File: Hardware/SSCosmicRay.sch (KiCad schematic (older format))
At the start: 0 parts

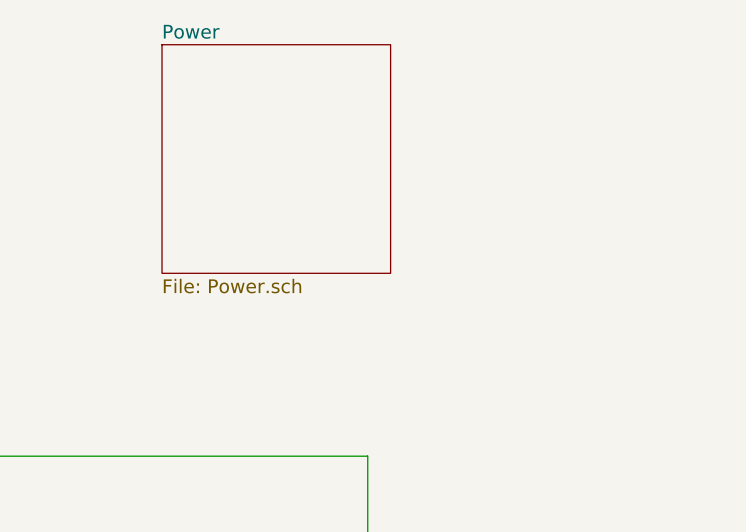
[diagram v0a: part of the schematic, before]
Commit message: Add power section. Switch to smaller pot
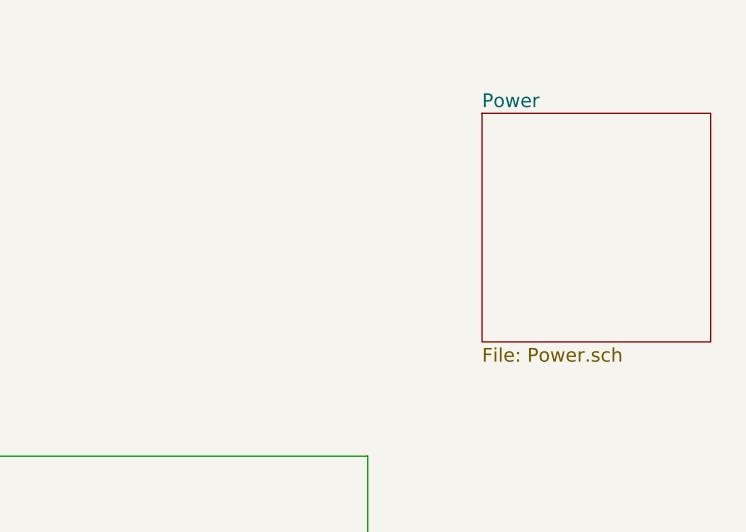
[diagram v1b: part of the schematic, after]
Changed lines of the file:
@@
 $Descr A4 11693 8268
 encoding utf-8
-Sheet 1 7
+Sheet 1 8
 Title "Solid State Cosmic Ray Detector"
 Date "24 sep 2013"
@@
 Connection ~ 5900 4900
 $Sheet
-S 7000 1100 1000 1000
+S 8400 1400 1000 1000
 U 5241F320
 F0 "Power" 60

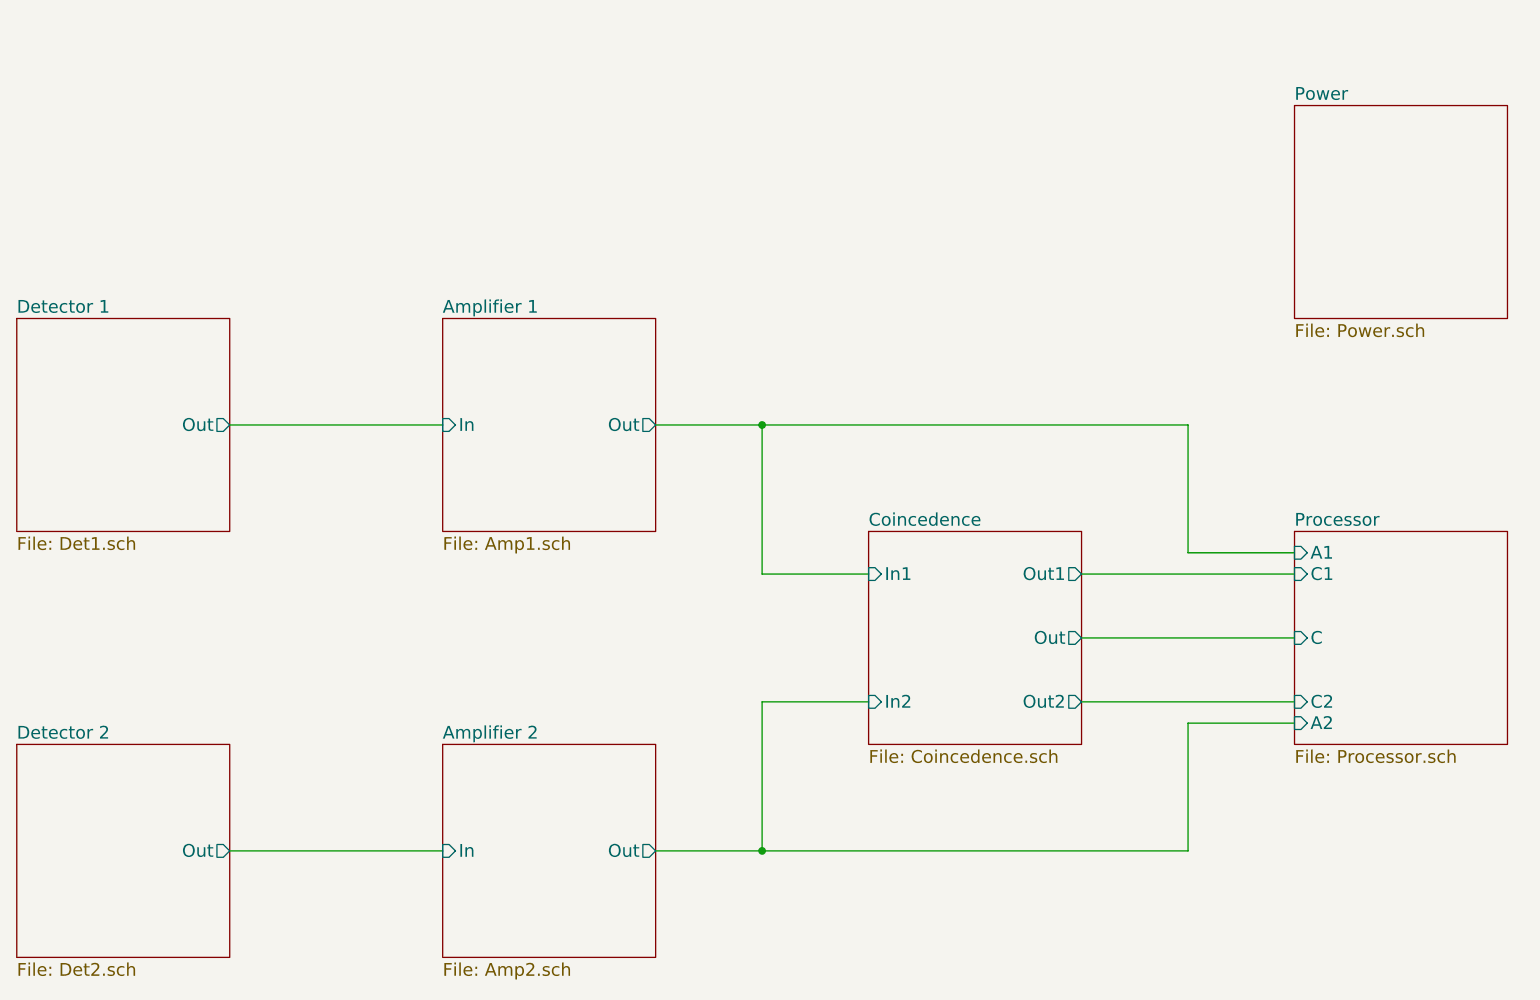
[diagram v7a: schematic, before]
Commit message: Remove coincidence circuitry
PIC32 internal comparator has sufficient performance
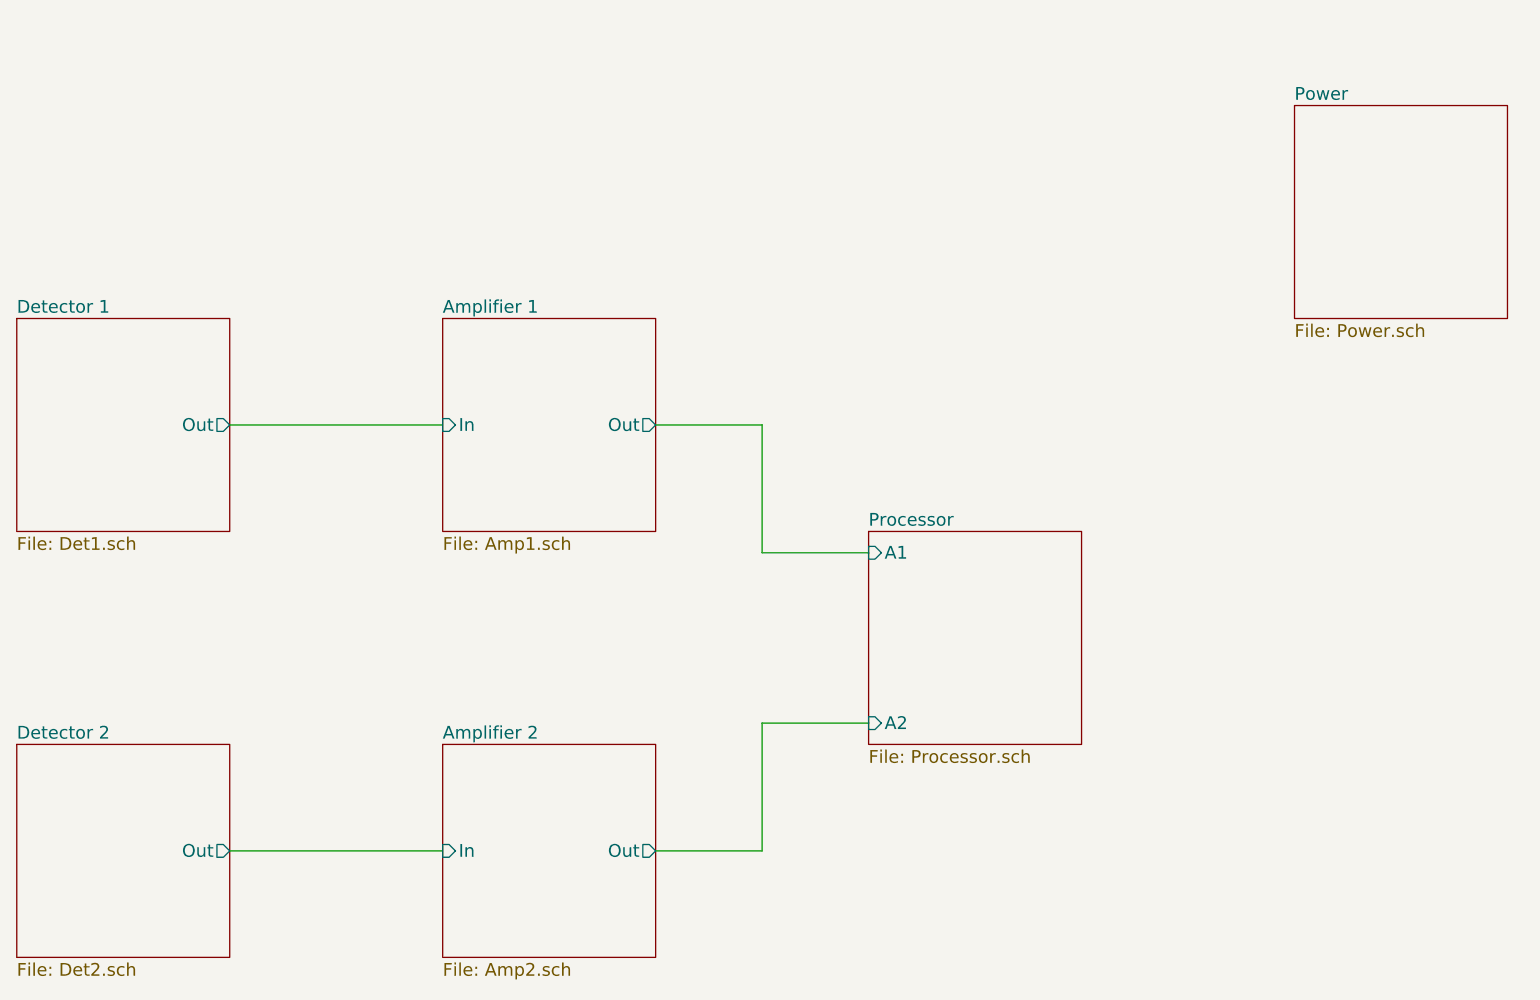
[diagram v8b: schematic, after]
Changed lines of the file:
@@
 $Descr A4 11693 8268
 encoding utf-8
-Sheet 1 8
+Sheet 1 7
 Title "Solid State Cosmic Ray Detector"
-Date "22 dec 2013"
+Date "24 dec 2013"
 Rev "1"
 Comp "Ethan Harstad"
@@
 Wire Wire Line
 	3400 2900 4400 2900
+Wire Wire Line
+	5400 2900 5900 2900
 $Sheet
 S 6400 3400 1000 1000
-U 523E0DA4
-F0 "Coincedence" 60
-F1 "Coincedence.sch" 60
-F2 "In1" I L 6400 3600 60
-F3 "In2" I L 6400 4200 60
-F4 "Out1" O R 7400 3600 60
-F5 "Out2" O R 7400 4200 60
-F6 "Out" O R 7400 3900 60
-$EndSheet
-Wire Wire Line
-	5400 2900 7900 2900
-Wire Wire Line
-	5900 2900 5900 3600
-Wire Wire Line
-	5900 3600 6400 3600
-$Sheet
-S 8400 3400 1000 1000
 U 523FD5E2
 F0 "Processor" 60
 F1 "Processor.sch" 60
-F2 "C" I L 8400 3900 60
-F3 "C1" I L 8400 3600 60
-F4 "C2" I L 8400 4200 60
-F5 "A1" I L 8400 3500 60
-F6 "A2" I L 8400 4300 60
+F2 "A1" I L 6400 3500 60
+F3 "A2" I L 6400 4300 60
 $EndSheet
 Wire Wire Line
-	7400 3600 8400 3600
+	5900 2900 5900 3500
 Wire Wire Line
-	7400 3900 8400 3900
-Wire Wire Line
-	7400 4200 8400 4200
-Wire Wire Line
-	7900 2900 7900 3500
-Wire Wire Line
-	7900 3500 8400 3500
-Connection ~ 5900 2900
+	5900 3500 6400 3500
 $Sheet
 S 4400 4400 1000 1000
@@
 	3400 4900 4400 4900
 Wire Wire Line
-	5400 4900 7900 4900
+	5400 4900 5900 4900
 Wire Wire Line
-	5900 4900 5900 4200
+	5900 4900 5900 4300
 Wire Wire Line
-	5900 4200 6400 4200
-Wire Wire Line
-	7900 4900 7900 4300
-Wire Wire Line
-	7900 4300 8400 4300
-Connection ~ 5900 4900
+	5900 4300 6400 4300
 $Sheet
 S 8400 1400 1000 1000
